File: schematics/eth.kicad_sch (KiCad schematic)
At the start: 44 parts, among them J5 Bus_RJ45_5-2337992-8, Q7 DTC014T_SOT-416, Q8 DTC014T_SOT-416, U22 DP83867CR_VQFN, Y2 Oscillator_25MHz_ESC_2016MV

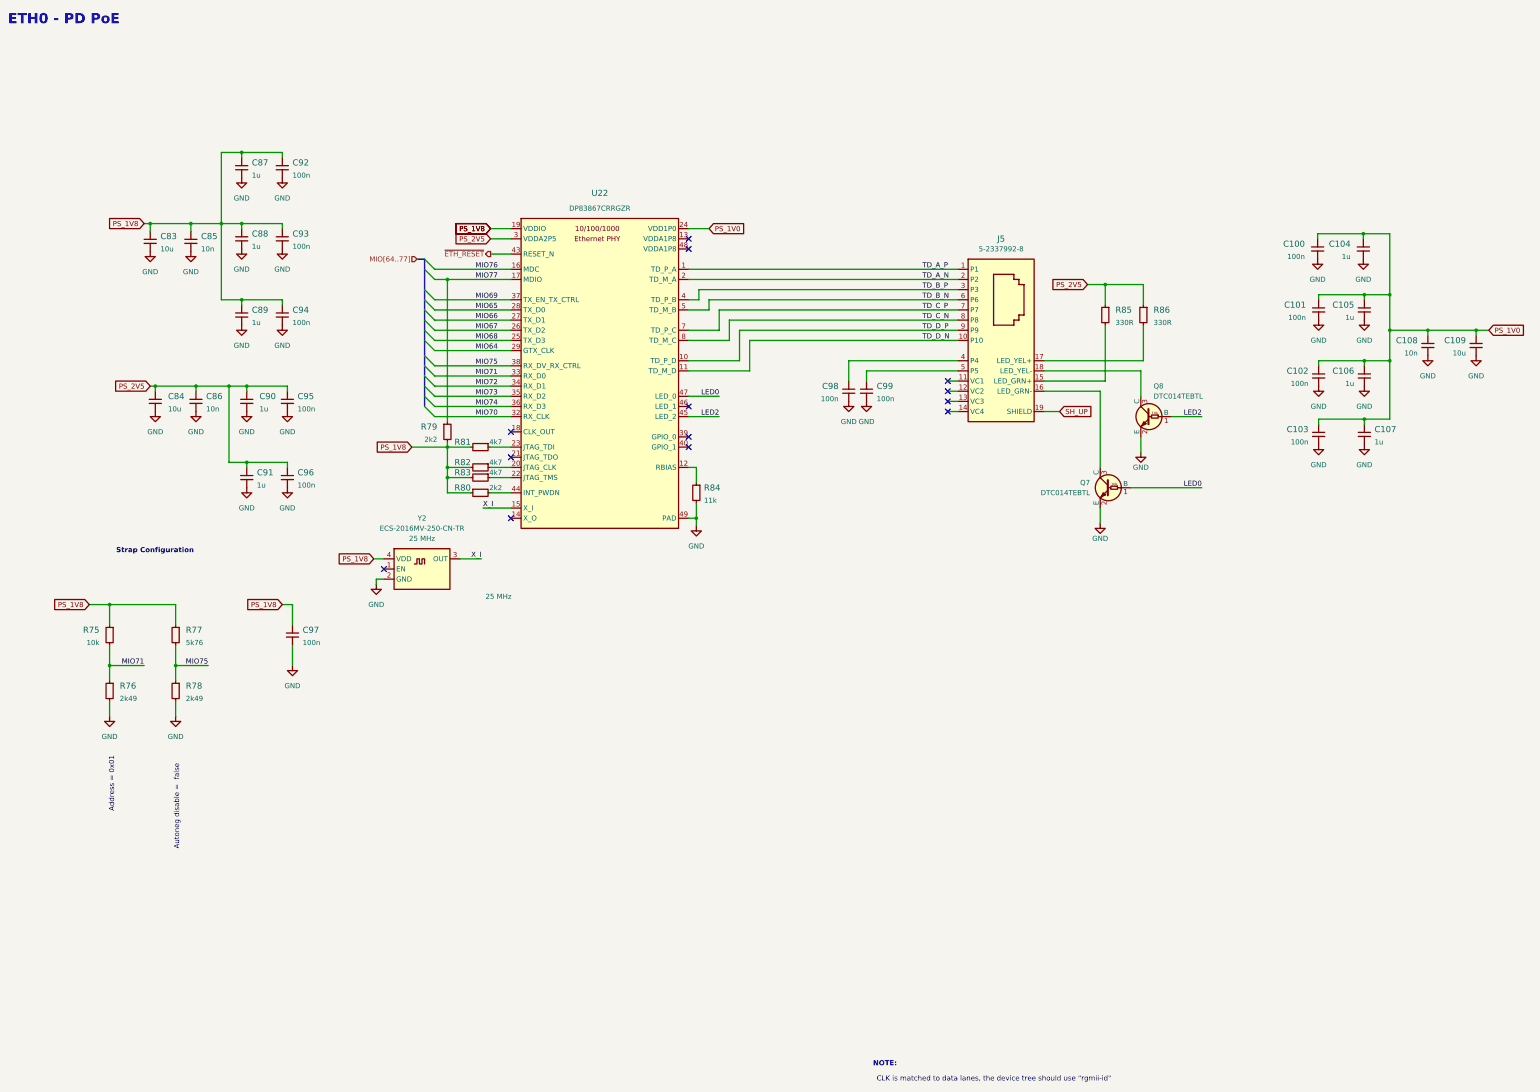
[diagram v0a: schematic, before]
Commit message: Voltage converter added
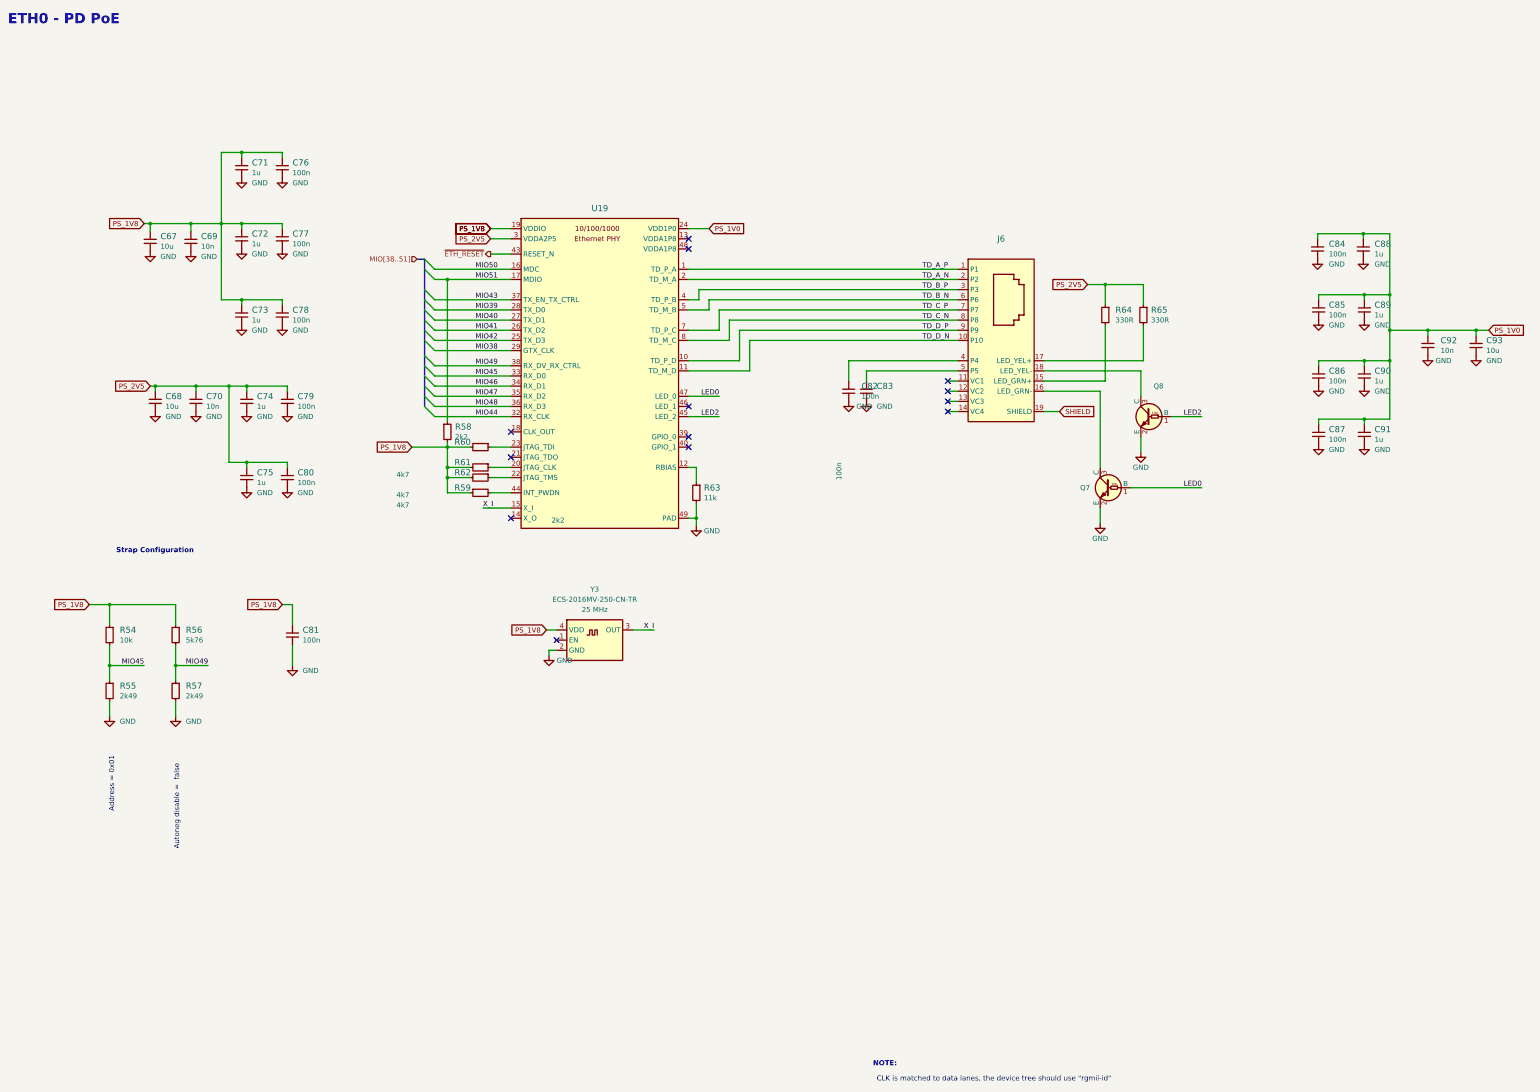
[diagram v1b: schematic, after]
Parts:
- C67: renamed from C83; Dielectric (none) -> template_dielectric
- C68: renamed from C84; Dielectric (none) -> template_dielectric
- C93: renamed from C109; Dielectric (none) -> template_dielectric
- Y3: renamed from Y2; VAL 25 MHz -> (none)
- renumbered C85 to C69, C86 to C70, C87 to C71, C88 to C72, C89 to C73, C90 to C74, C91 to C75, C92 to C76, C93 to C77, C94 to C78, C95 to C79, C96 to C80, C97 to C81, C98 to C82, C99 to C83, C100 to C84, C101 to C85, C102 to C86, C103 to C87, C104 to C88, C105 to C89, C106 to C90, C107 to C91, C108 to C92, J5 to J6, R75 to R54, R76 to R55, R77 to R56, R78 to R57, R79 to R58, R80 to R59, R81 to R60, R82 to R61, R83 to R62, R84 to R63, R85 to R64, R86 to R65, U22 to U19
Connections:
- net MIO64 renamed MIO38
- net MIO65 renamed MIO39
- net MIO66 renamed MIO40
- net MIO67 renamed MIO41
- net MIO68 renamed MIO42
- net MIO69 renamed MIO43
- net MIO70 renamed MIO44
- net MIO71 renamed MIO45
- net MIO72 renamed MIO46
- net MIO73 renamed MIO47
- net MIO74 renamed MIO48
- net MIO75 renamed MIO49
- net MIO76 renamed MIO50
- net MIO77 renamed MIO51
- net SH_UP renamed SHIELD
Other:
- moved on the sheet: Y3
